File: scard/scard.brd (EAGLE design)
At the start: 160 x 100 mm, 68 parts, among them Q1 IRFD9210, X1 COAX

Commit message: first stage of layout for power systems
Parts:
- added C21: 10uF, resistor:C0603
- Q1: value IRFD9210 -> FDN360P; device transistor-fet:DIL04 -> transistor-power:SUPER-SOT3
- R14, R15, R18, R19: device resistor:R0603 -> resistor:R1210
- R9: value (none) -> 10k
- moved R26 305.1 mm to (66.0, 21.6)
- moved R28 305.1 mm to (66.0, 16.5)
- moved R29 305.1 mm to (71.1, 16.5)
- moved R30 305.1 mm to (66.0, 11.4)
- moved R31 305.1 mm to (71.1, 11.4)
- moved R32 305.1 mm to (66.0, 6.35)
- moved R33 305.1 mm to (66.0, 1.27)
- moved R14 301.2 mm to (35.5, 88.6), turned to 270 degrees
- moved R15 294.8 mm to (35.8, 75.9), turned to 270 degrees
- moved R27 287.8 mm to (61.0, 7.62)
- moved R24 278.4 mm to (47.0, 12.7)
- moved R25 277.5 mm to (52.1, 2.54)
- moved R23 275.1 mm to (54.6, 7.62)
- moved L3 274.9 mm to (139.7, 11.4)
- moved R18 274.9 mm to (3.24, 66.3), turned to 270 degrees
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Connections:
- net +3V3: now also C21.1; no longer Q1.4
- net GND: now also C21.2
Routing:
- net SYS_UNREG: track 0.00 -> 124.4 mm
- net REG0_3V3: track 0.00 -> 65.0 mm, vias 0 -> 2
- net REG1_3V3: track 0.00 -> 60.1 mm, vias 0 -> 2
- net GND: track 0.00 -> 28.1 mm
- net N$11: track 0.00 -> 26.0 mm, vias 0 -> 4
- net N$12: track 0.00 -> 21.3 mm, vias 0 -> 4
- net +3V3: track 0.00 -> 20.3 mm
- net N$15: track 0.00 -> 14.9 mm, vias 0 -> 4
- net N$13: track 0.00 -> 13.4 mm, vias 0 -> 4
- net SYS_UNREG_CUR: track 0.00 -> 13.0 mm
- net REG1_EN: track 0.00 -> 6.18 mm
- net REG0_EN: track 0.00 -> 5.17 mm
- net N$10: track 0.00 -> 3.89 mm
- net N$14: track 0.00 -> 3.74 mm
- net REG0_PGOOD: track 0.00 -> 2.52 mm
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
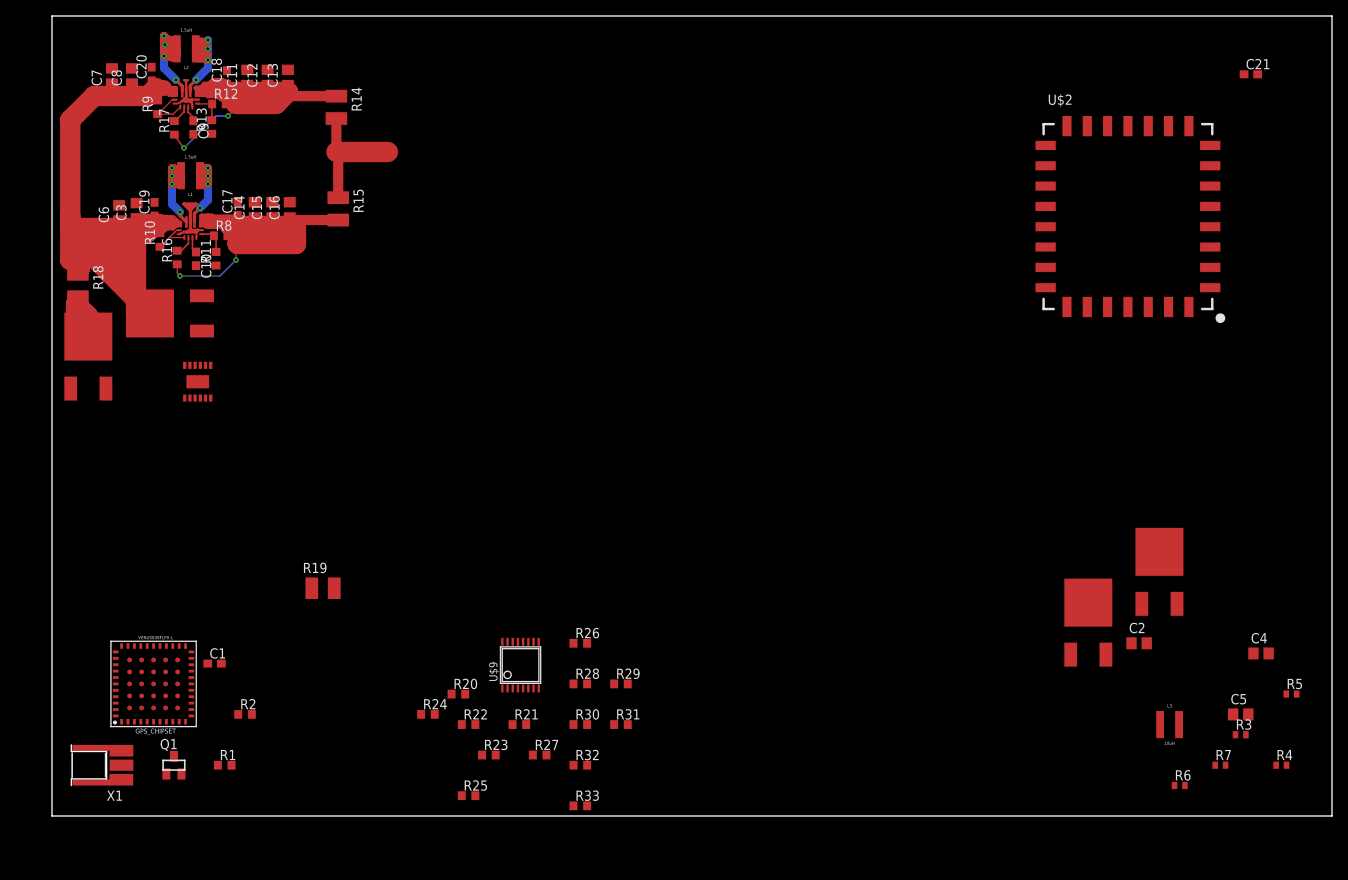
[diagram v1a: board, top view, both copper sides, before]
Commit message: finished test board v0.1 layout and added pictures
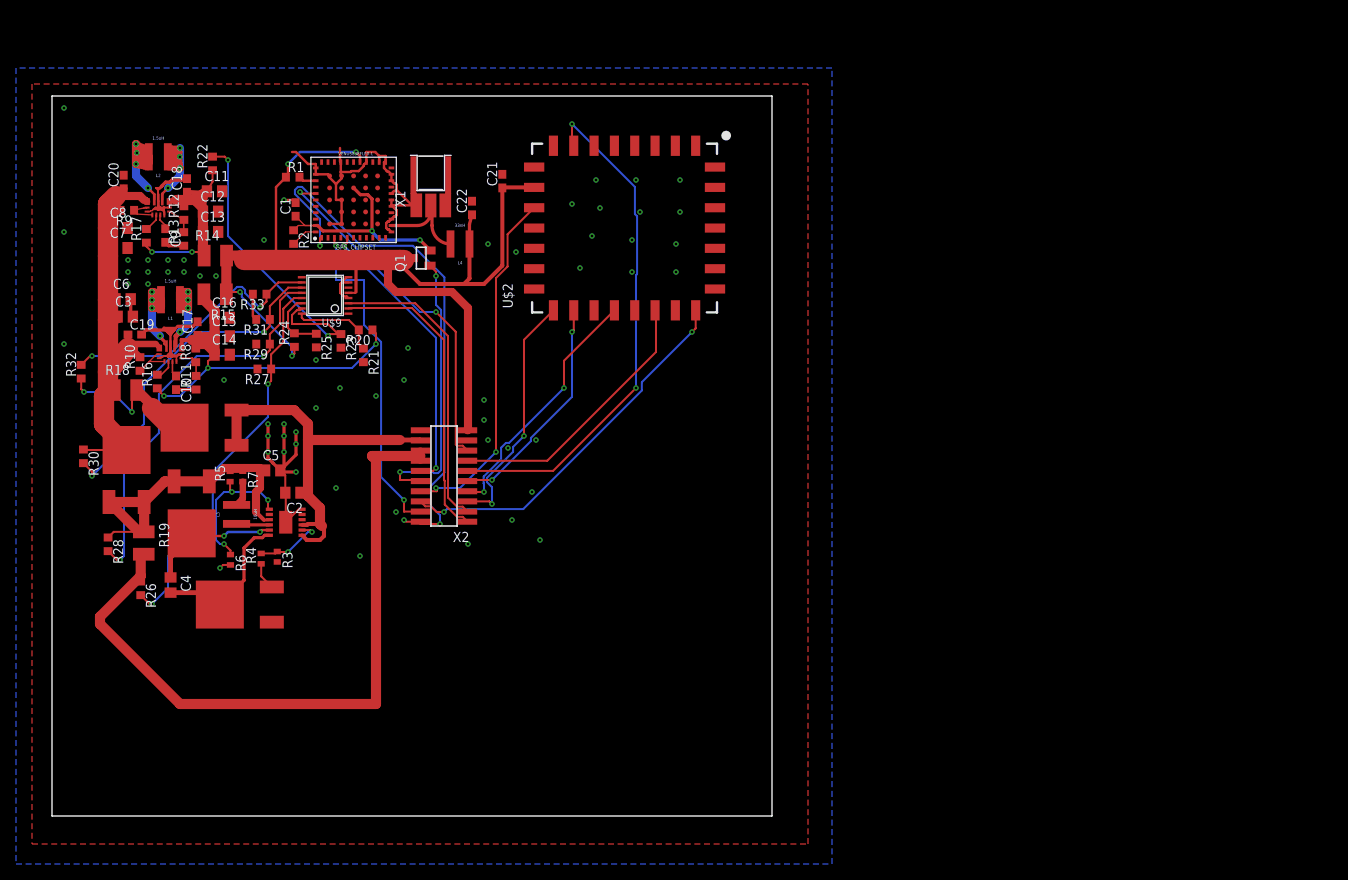
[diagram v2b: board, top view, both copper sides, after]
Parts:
- added C22: 10uF, resistor:C0603
- added L4: 33nH, calsat:XFL4020
- added X2: 1365-20, con-leotronics:1365-20
- moved C4 136.6 mm to (14.8, 28.9), turned to 270 degrees
- moved R5 135.4 mm to (22.3, 42.4), turned to 90 degrees
- moved R4 130.1 mm to (26.1, 32.2), turned to 90 degrees
- moved R7 127.4 mm to (23.9, 42.5), turned to 270 degrees
- moved C5 124.8 mm to (27.6, 43.2)
- moved R3 122.5 mm to (28.2, 32.4), turned to 270 degrees
- moved R6 122.0 mm to (22.3, 32.0), turned to 270 degrees
- moved L3 119.6 mm to (23.1, 37.7), turned to 90 degrees
- moved U$5 117.6 mm to (21.0, 26.4), turned to 90 degrees
- moved U$3 112.4 mm to (17.5, 35.3), turned to 180 degrees
- moved C2 107.4 mm to (30.1, 40.4), turned to 180 degrees
- moved C21 94.5 mm to (56.3, 79.4), turned to 90 degrees
- moved X1 88.3 mm to (47.4, 82.5), turned to 0 degrees
- moved R32 79.4 mm to (3.65, 55.5), turned to 90 degrees
- moved R22 77.1 mm to (20.1, 81.6), turned to 90 degrees
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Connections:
- net +12V: now also X2.18
- net +3V3: now also C22.1, L4.1, X2.19; no longer X1.2@1
- net ANT_IN: now also L4.2
- net GND: now also C22.2, C3.2, X1.2@1, X2.17, X2.20
- net GPS_EN: now also X2.10
- net I2C_SCL: now also X2.3
- net I2C_SDA: now also X2.1
- net IMU_CS: now also X2.6
- net IMU_EN: now also X2.8
- net IMU_RST: now also X2.13
- net N$19: now also U$9.13
- net N$20: now also U$9.12
- net P1PPS: now also X2.12
- net SPI_MISO: now also X2.7
- net SPI_MOSI: now also X2.9
- net SPI_SCK: now also X2.5
- net STS: now also X2.15
- net TARE_GPIO: now also X2.11
- net UART0_RXD: now also X2.2
- net UART0_TXD: now also X2.4
- net VBATT: now also X2.14, X2.16
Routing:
- net +3V3: track 20.3 -> 155.7 mm, vias 0 -> 4
- net GND: track 28.1 -> 140.2 mm, vias 0 -> 61
- net VBATT: track 0.00 -> 88.8 mm
- net UART0_RXD: track 0.00 -> 70.0 mm, vias 0 -> 3
- net TARE_GPIO: track 0.00 -> 64.6 mm, vias 0 -> 2
- net SYS_UNREG: track 124.4 -> 65.2 mm
- net N$20: track 0.00 -> 50.7 mm, vias 0 -> 2
- net +12V: track 0.00 -> 49.5 mm
- net N$19: track 0.00 -> 48.4 mm, vias 0 -> 2
- net IMU_CS: track 0.00 -> 47.3 mm, vias 0 -> 2
- net VBATT_CUR: track 0.00 -> 45.8 mm
- net STS: track 0.00 -> 44.6 mm, vias 0 -> 2
- net IMU_EN: track 0.00 -> 44.3 mm, vias 0 -> 2
- net N$21: track 0.00 -> 42.4 mm, vias 0 -> 2
- net UART0_TXD: track 0.00 -> 42.0 mm, vias 0 -> 2
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- added copper zone on layer 1, net GND
- added copper zone on layer 16, net GND
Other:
- board size 160 x 100 mm -> 90 x 90 mm
